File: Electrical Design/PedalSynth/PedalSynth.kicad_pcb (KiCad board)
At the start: 2 copper layers, 68.2 x 40.5 mm, 27 parts, among them J1 AudioJack3, J2 speakON_NL2MDXX-V, J3 Barrel_Jack, U1 TPA3136D2PWPR

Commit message: update to v8
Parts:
- removed J2: speakON_NL2MDXX-V, Connector_Audio:Jack_speakON_Neutrik_NL2MDXX-H-3_Horizontal
- removed L1, L2: 33u, Inductor_SMD:L_Taiyo-Yuden_MD-3030
- removed R4: 56k, Resistor_SMD:R_0402_1005Metric_Pad0.72x0.64mm_HandSolder
- added RV1: 100k, Potentiometer_THT:Potentiometer_Bourns_3386P_Vertical, F.Cu at (132.1, 75.0)
- added TP1: TestPoint, TestPoint:TestPoint_Bridge_Pitch2.0mm_Drill0.7mm, F.Cu at (81.6, 76.1)
- added TP2: TestPoint, TestPoint:TestPoint_Bridge_Pitch2.0mm_Drill0.7mm, F.Cu at (81.6, 79.5)
- added TPSP+: TestPoint, TestPoint:TestPoint_Bridge_Pitch2.0mm_Drill0.7mm, F.Cu at (167.9, 69.5)
- added TPSP-: TestPoint, TestPoint:TestPoint_Bridge_Pitch2.0mm_Drill0.7mm, F.Cu at (165.9, 80.0)
- C1, C2: footprint Capacitor_THT:CP_Radial_D10.0mm_P5.00mm_P7.50mm -> Capacitor_THT:CP_Radial_D8.0mm_P3.50mm
- R3: value 39k -> 10k
- moved C13 9.85 mm to (157.8, 73.8)
- moved C14 9.85 mm to (157.8, 79.8)
- moved C6 8.91 mm to (150.9, 71.0)
- moved U1 8.91 mm to (147.5, 76.8)
- moved ? 8.91 mm to (173.0, 82.8)
- moved C3 8.91 mm to (156.0, 69.2)
- moved C4 8.91 mm to (156.0, 84.2)
- moved C5 8.91 mm to (140.9, 74.8)
- moved C7 8.91 mm to (150.8, 82.5)
- moved R1 8.91 mm to (141.7, 71.8)
- moved R2 8.91 mm to (142.2, 82.8)
- moved R5 8.91 mm to (139.3, 81.5)
- moved R6 8.91 mm to (139.4, 80.2)
- moved C1 8.86 mm to (159.4, 65.0)
- moved C10 8.81 mm to (142.2, 79.8)
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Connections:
- R3 pad 2: Net-(U1-PLIMIT) -> Net-(R3-Pad2)
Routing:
- net GND: track 149.0 -> 53.0 mm, vias 107 -> 90
- net VCC: track 175.5 -> 139.1 mm, vias 0 -> 1
- net /GVDD: track 8.38 -> 13.7 mm
- net Net-(U1-PLIMIT): track 10.5 -> 15.5 mm
- net Net-(R3-Pad2): track 0.00 -> 4.50 mm
- net /BSPL: track 0.00 -> 4.32 mm, vias 0 -> 1
- net Net-(J1-PadT): track 22.3 -> 25.6 mm
- net /SPK+: track 21.0 -> 24.1 mm
- net /OUTPR: track 8.21 -> 5.68 mm
- net /OUTPL: track 8.12 -> 5.86 mm
- net /SPK-: track 22.0 -> 24.2 mm
- net Net-(J1-PadR): track 7.74 -> 9.56 mm
- net /BSNR: track 2.53 -> 4.23 mm, vias 0 -> 1
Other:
- board size 68.2 x 40.5 mm -> 71.9 x 39 mm

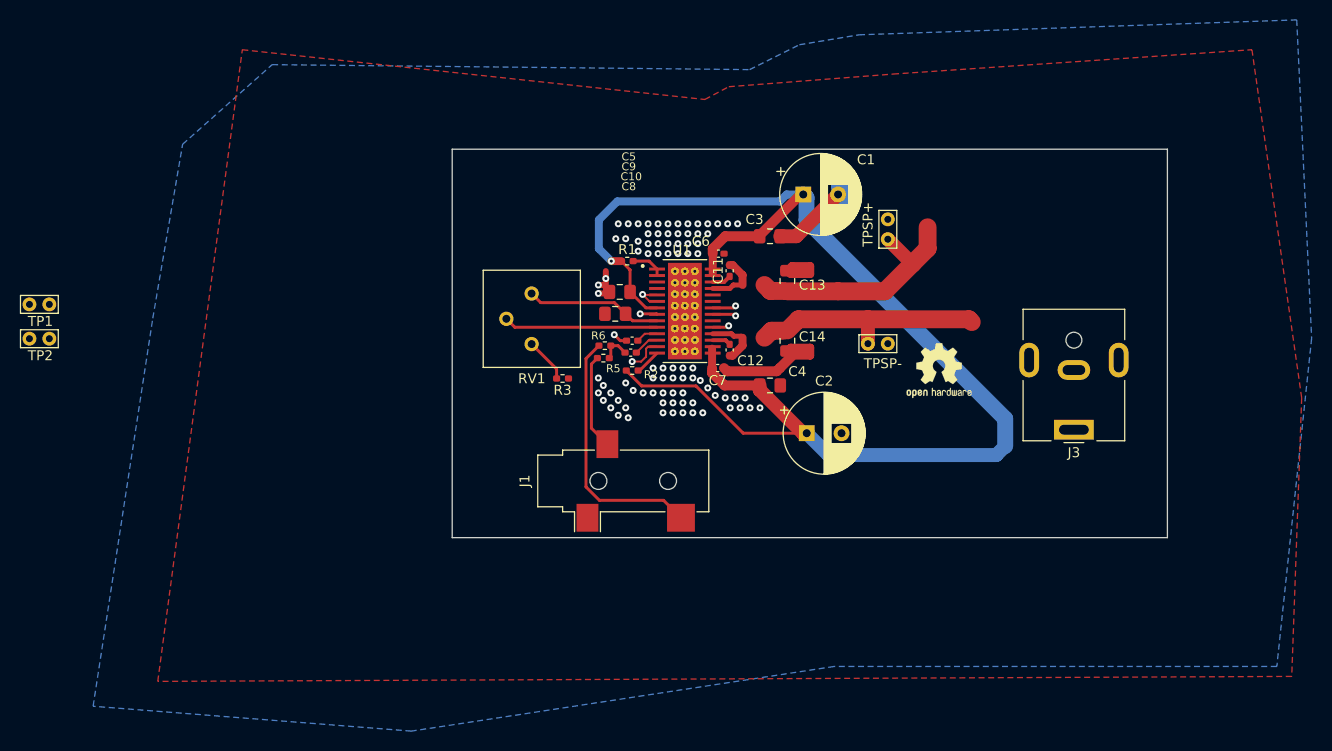
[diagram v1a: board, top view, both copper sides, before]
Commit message: update amp schematic and pcb
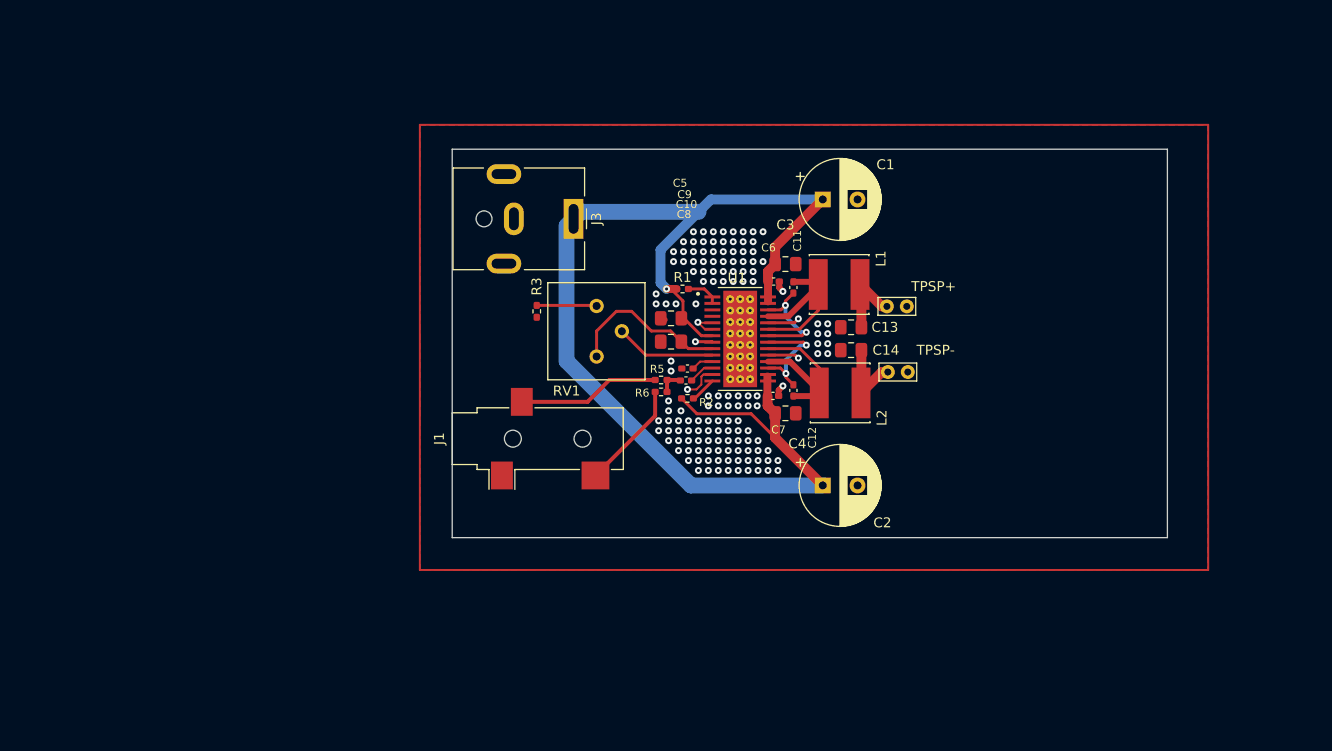
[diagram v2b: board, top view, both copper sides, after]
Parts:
- removed ?: , clipboard:c860e70c-6b6c-4b37-9969-0fdff2164b0f
- removed TP1, TP2: TestPoint, TestPoint:TestPoint_Bridge_Pitch2.0mm_Drill0.7mm
- added L1: 33u, VLS6045AF_330M:IND_VLS6045AF-330M, F.Cu at (163.0, 74.1)
- added L2: 33u, VLS6045AF_330M:IND_VLS6045AF-330M, F.Cu at (163.1, 85.0)
- moved J3 54.6 mm to (136.3, 67.5), turned to -90 degrees
- moved J1 9.59 mm to (132.7, 89.6)
- moved RV1 9.09 mm to (138.6, 81.3), turned to 0 degrees
- moved C13 7.92 mm to (164.2, 78.4), turned to 180 degrees
- moved C12 7.59 mm to (158.4, 84.8)
- moved R6 7.32 mm to (145.1, 84.9)
- moved R3 7.23 mm to (132.6, 76.8), turned to 90 degrees
- moved TPSP+ 6.75 mm to (167.8, 76.3), turned to 0 degrees
- moved C11 6.62 mm to (158.4, 74.4)
- moved C14 6.48 mm to (164.2, 80.7), turned to 180 degrees
- moved C9 6.27 mm to (146.1, 79.8)
- moved C10 6.22 mm to (147.8, 82.5)
- moved C7 6.22 mm to (156.3, 85.3)
- moved C8 6.22 mm to (147.6, 83.8)
- moved R1 6.22 mm to (147.3, 74.5)
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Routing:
- net GND: track 53.0 -> 18.9 mm, vias 90 -> 143
- net /SPK-: track 24.2 -> 7.89 mm
- net /SPK+: track 24.1 -> 7.97 mm
- net Net-(J1-PadT): track 25.6 -> 10.9 mm
- net /OUTPR: track 5.68 -> 18.9 mm
- net /OUTPL: track 5.86 -> 17.5 mm
- net /BSNR: track 4.23 -> 11.5 mm, vias 1 -> 2
- net /BSPL: track 4.32 -> 11.4 mm, vias 1 -> 2
- net Net-(U1-PLIMIT): track 15.5 -> 10.1 mm
- net VCC: track 139.1 -> 134.0 mm
- net Net-(J1-PadR): track 9.56 -> 14.3 mm
- net /GVDD: track 13.7 -> 16.6 mm
- net Net-(R3-Pad2): track 4.50 -> 6.04 mm

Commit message: r1.0 amp pcb
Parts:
- added G***: LOGO, LOGO, F.Cu at (181.3, 92.6)
- added G***: LOGO, LOGO, F.Cu at (173.1, 96.7)
- added GND1: TestPoint, TestPoint:TestPoint_Bridge_Pitch2.0mm_Drill0.7mm, F.Cu at (125.8, 79.9)
- added J2: Pheonix Latching Connector (1190297), Pheonix-2P-Level1190297:PHOENIX_1190297, F.Cu at (185.1, 85.0)
- added RING1: TestPoint, TestPoint:TestPoint_Bridge_Pitch2.0mm_Drill0.7mm, F.Cu at (144.1, 97.0)
- added SLEEVE1: TestPoint, TestPoint:TestPoint_Bridge_Pitch2.0mm_Drill0.7mm, F.Cu at (150.6, 97.0)
- moved TPSP1 4.55 mm to (169.3, 72.0)
- moved TPSP2 4.16 mm to (169.3, 86.8)
- moved J1 1.70 mm to (132.7, 91.3)
- moved C1 0.35 mm to (161.3, 65.9)
- moved C8 0.21 mm to (147.8, 83.6)
- moved L1 0.10 mm to (163.1, 74.1)
- renumbered TPSP+ to TPSP1, TPSP- to TPSP2
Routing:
- net Net-(J1-PadR): track 14.3 -> 36.1 mm
- net /SPK+: track 7.97 -> 27.0 mm
- net /SPK-: track 7.89 -> 26.6 mm
- net Net-(J1-PadT): track 10.9 -> 27.5 mm
- net GND: track 18.9 -> 19.5 mm, vias 143 -> 275
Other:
- board size 71.9 x 39 mm -> 61 x 39 mm
- board text added: "4.5-14.4 VDC"
- board text added: "AUX IN"
- board text added: "Design: Eric Sanman Portland, OR"
- board text added: "Mono 20 W Class-D Audio Amplifier TI TPA3136"
- board text added: "OUT"
- board text added: "P_{LIMIT}"

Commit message: update stuff
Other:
- board text added: "8-14.4 VDC"
- board text removed: "4.5-14.4 VDC"
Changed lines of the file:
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@@
 		)
 	)
-	(gr_text "4.5-14.4\nVDC"
+	(gr_text "8-14.4\nVDC"
 		(at 124.85 76.8 0)
 		(layer "F.SilkS" knockout)
